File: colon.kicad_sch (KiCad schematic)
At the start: 10 parts, among them U42 SN74LVC244A

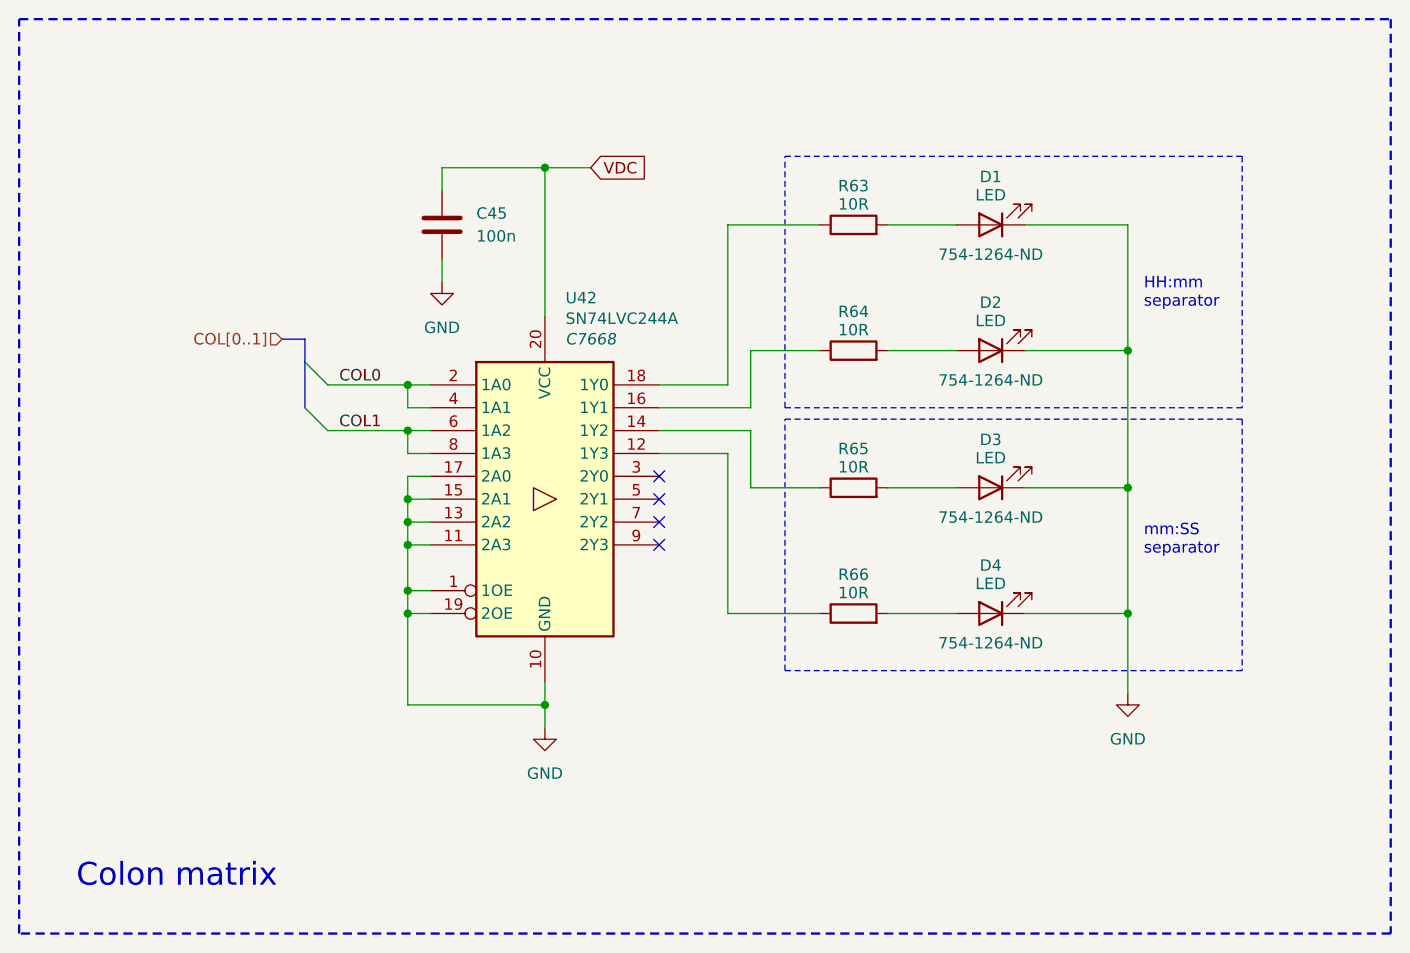
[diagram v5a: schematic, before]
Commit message: PCB routing
- JLCPCB constraints added
- removal of multiple test points
- change of footprints
- change of THT LEDs
- rough position of all the major components
- PCB routing started
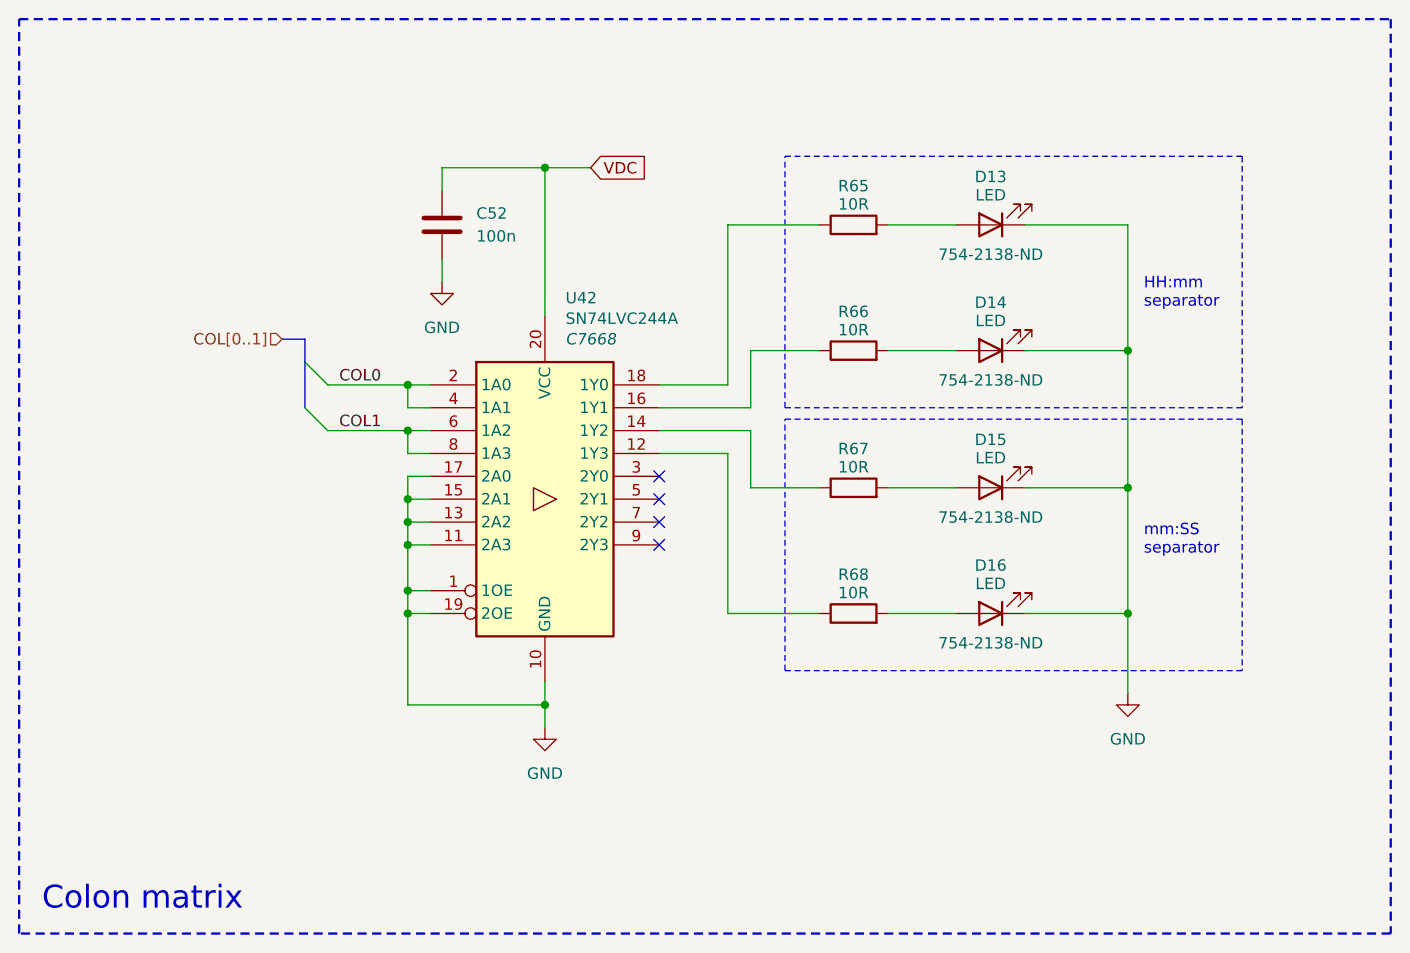
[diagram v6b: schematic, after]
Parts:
- removed D2, D3, D4: LED, LED_THT:LED_D5.0mm, symbol Device:LED
- added D14, D15, D16: LED, LED_THT:LED_D5.0mm, symbol Device:LED
- D13: renamed from D1; Digikey 754-1264-ND -> 754-2138-ND
- renumbered C45 to C52, R63 to R65, R64 to R66, R65 to R67, R66 to R68
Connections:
- net GND: now also D14.1 (K), D15.1 (K), D16.1 (K)
- net at R66.2: now also D14.2 (A)
- net at R67.2: now also D15.2 (A)
- net at R68.2: now also D16.2 (A)

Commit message: PCB routing
- addition of 3D models
- addition of docs
- reduction of the size of passives
- increase in size of traces
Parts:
- C52: footprint Capacitor_SMD:C_0603_1608Metric -> Capacitor_SMD:C_0402_1005Metric
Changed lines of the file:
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@@
 			)
 		)
-		(property "Footprint" "Capacitor_SMD:C_0603_1608Metric"
+		(property "Footprint" "Capacitor_SMD:C_0402_1005Metric"
 			(at 111.4552 77.47 0)
 			(effects

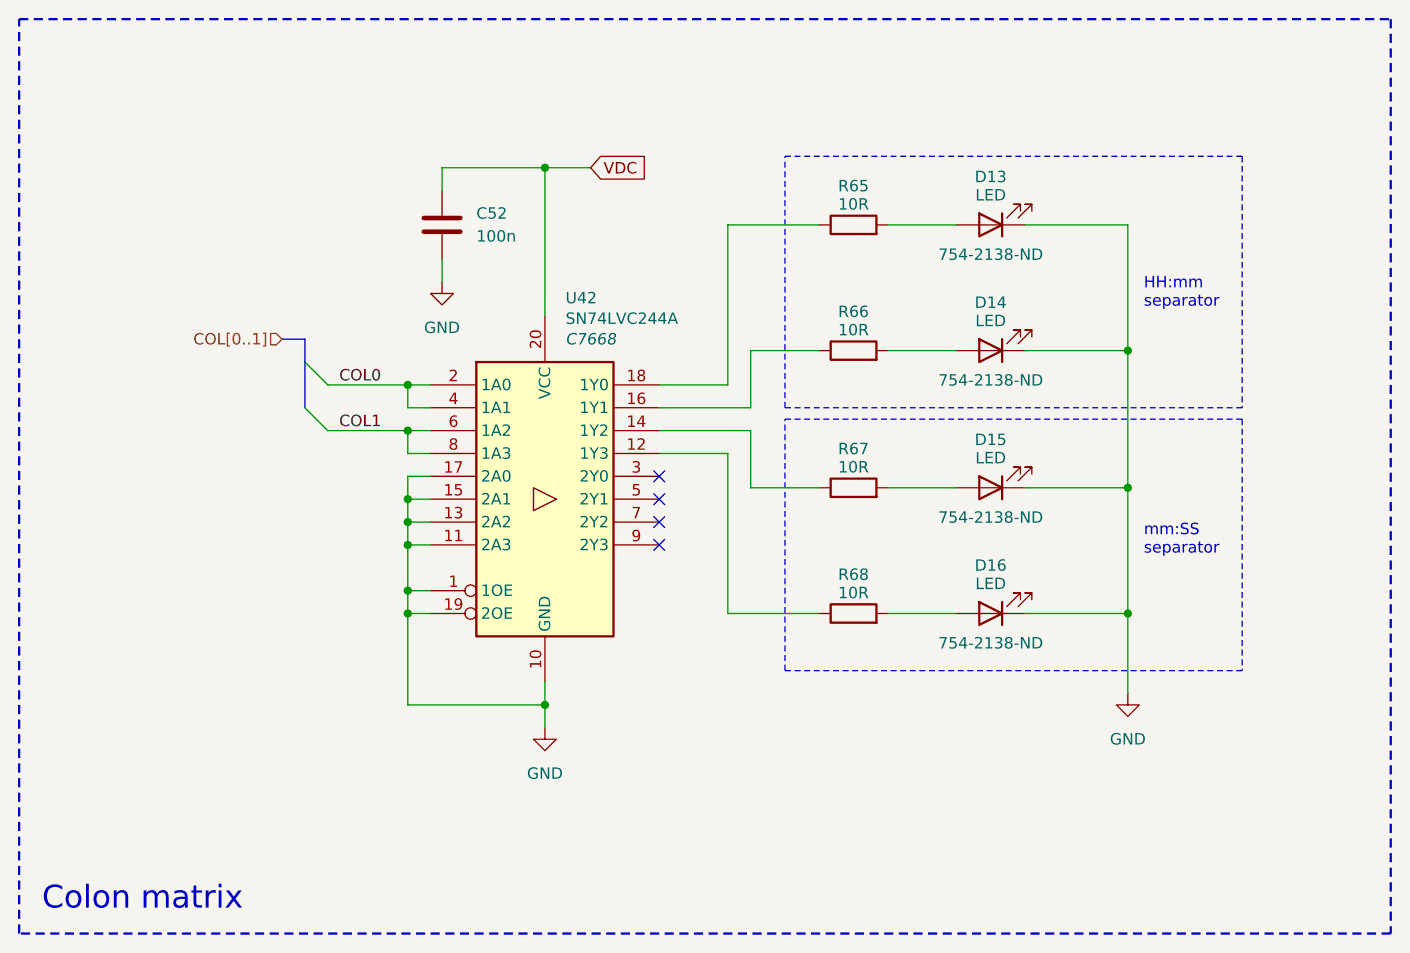
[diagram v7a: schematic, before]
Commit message: Primary MCU rerouting
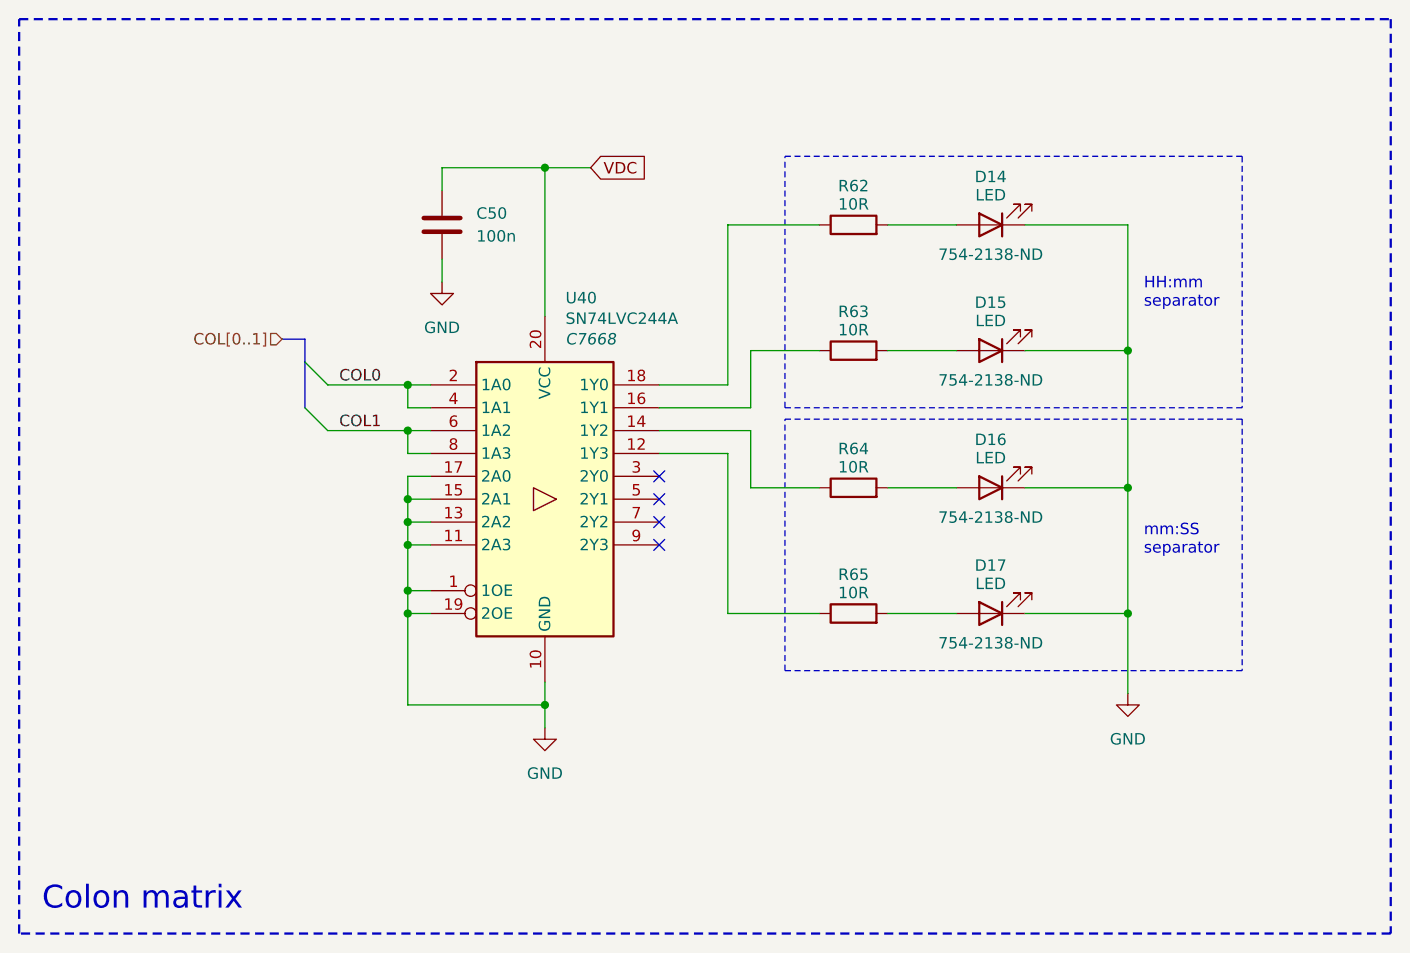
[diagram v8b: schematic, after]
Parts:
- renumbered C52 to C50, D13 to D14, D14 to D15, D15 to D16, D16 to D17, R65 to R62, R66 to R63, R67 to R64, R68 to R65, U42 to U40
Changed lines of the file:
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@@
 		(on_board yes)
 		(dnp no)
-		(property "Reference" "D16"
+		(property "Reference" "D17"
 			(at 171.45 111.506 0)
 			(effects
@@
 			(project "Precision Clock"
 				(path "/c9a8ff63-a0d1-4125-9dd1-40fb53daf536/9ee9cf55-854a-46a7-9bd0-7970985d5955"
-					(reference "D16")
+					(reference "D17")
 					(unit 1)
 				)
@@
 		(dnp no)
 		(fields_autoplaced yes)
-		(property "Reference" "#PWR0116"
+		(property "Reference" "#PWR0108"
 			(at 110.49 86.36 0)
 			(effects
@@
 			(project "Precision Clock"
 				(path "/c9a8ff63-a0d1-4125-9dd1-40fb53daf536/9ee9cf55-854a-46a7-9bd0-7970985d5955"
-					(reference "#PWR0116")
+					(reference "#PWR0108")
 					(unit 1)
 				)
@@
 		(on_board yes)
 		(dnp no)
-		(property "Reference" "D15"
+		(property "Reference" "D16"
 			(at 171.45 97.536 0)
 			(effects
@@
 			(project "Precision Clock"
 				(path "/c9a8ff63-a0d1-4125-9dd1-40fb53daf536/9ee9cf55-854a-46a7-9bd0-7970985d5955"
-					(reference "D15")
+					(reference "D16")
 					(unit 1)
 				)
@@
 		(on_board yes)
 		(dnp no)
-		(property "Reference" "R66"
+		(property "Reference" "R63"
 			(at 156.21 83.312 90)
 			(effects
@@
 			(project "Precision Clock"
 				(path "/c9a8ff63-a0d1-4125-9dd1-40fb53daf536/9ee9cf55-854a-46a7-9bd0-7970985d5955"
-					(reference "R66")
+					(reference "R63")
 					(unit 1)
 				)
@@
 		(on_board yes)
 		(dnp no)
-		(property "Reference" "D13"
+		(property "Reference" "D14"
 			(at 171.45 68.326 0)
 			(effects
@@
 			(project "Precision Clock"
 				(path "/c9a8ff63-a0d1-4125-9dd1-40fb53daf536/9ee9cf55-854a-46a7-9bd0-7970985d5955"
-					(reference "D13")
+					(reference "D14")
 					(unit 1)
 				)
@@
 		(on_board yes)
 		(dnp no)
-		(property "Reference" "U42"
+		(property "Reference" "U40"
 			(at 124.206 81.788 0)
 			(effects
@@
 			(project "Precision Clock"
 				(path "/c9a8ff63-a0d1-4125-9dd1-40fb53daf536/9ee9cf55-854a-46a7-9bd0-7970985d5955"
-					(reference "U42")
+					(reference "U40")
 					(unit 1)
 				)
@@
 		(dnp no)
 		(fields_autoplaced yes)
-		(property "Reference" "C52"
+		(property "Reference" "C50"
 			(at 114.3 72.3899 0)
 			(effects
@@
 			(project "Precision Clock"
 				(path "/c9a8ff63-a0d1-4125-9dd1-40fb53daf536/9ee9cf55-854a-46a7-9bd0-7970985d5955"
-					(reference "C52")
+					(reference "C50")
 					(unit 1)
 				)
@@
 		(on_board yes)
 		(dnp no)
-		(property "Reference" "R68"
+		(property "Reference" "R65"
 			(at 156.21 112.522 90)
 			(effects
@@
 			(project "Precision Clock"
 				(path "/c9a8ff63-a0d1-4125-9dd1-40fb53daf536/9ee9cf55-854a-46a7-9bd0-7970985d5955"
-					(reference "R68")
+					(reference "R65")
 					(unit 1)
 				)
@@
 		(on_board yes)
 		(dnp no)
-		(property "Reference" "D14"
+		(property "Reference" "D15"
 			(at 171.45 82.296 0)
 			(effects
@@
 			(project "Precision Clock"
 				(path "/c9a8ff63-a0d1-4125-9dd1-40fb53daf536/9ee9cf55-854a-46a7-9bd0-7970985d5955"
-					(reference "D14")
+					(reference "D15")
 					(unit 1)
 				)
@@
 		(dnp no)
 		(fields_autoplaced yes)
-		(property "Reference" "#PWR0117"
+		(property "Reference" "#PWR0109"
 			(at 121.92 135.89 0)
 			(effects
@@
 			(project "Precision Clock"
 				(path "/c9a8ff63-a0d1-4125-9dd1-40fb53daf536/9ee9cf55-854a-46a7-9bd0-7970985d5955"
-					(reference "#PWR0117")
+					(reference "#PWR0109")
 					(unit 1)
 				)
@@
 		(on_board yes)
 		(dnp no)
-		(property "Reference" "R67"
+		(property "Reference" "R64"
 			(at 156.21 98.552 90)
 			(effects
@@
 			(project "Precision Clock"
 				(path "/c9a8ff63-a0d1-4125-9dd1-40fb53daf536/9ee9cf55-854a-46a7-9bd0-7970985d5955"
-					(reference "R67")
+					(reference "R64")
 					(unit 1)
 				)
@@
 		(on_board yes)
 		(dnp no)
-		(property "Reference" "R65"
+		(property "Reference" "R62"
 			(at 156.21 69.342 90)
 			(effects
@@
 			(project "Precision Clock"
 				(path "/c9a8ff63-a0d1-4125-9dd1-40fb53daf536/9ee9cf55-854a-46a7-9bd0-7970985d5955"
-					(reference "R65")
+					(reference "R62")
 					(unit 1)
 				)
@@
 		(dnp no)
 		(fields_autoplaced yes)
-		(property "Reference" "#PWR0118"
+		(property "Reference" "#PWR0110"
 			(at 186.69 132.08 0)
 			(effects
@@
 			(project "Precision Clock"
 				(path "/c9a8ff63-a0d1-4125-9dd1-40fb53daf536/9ee9cf55-854a-46a7-9bd0-7970985d5955"
-					(reference "#PWR0118")
-					(unit 1)
-				)
+					(reference "#PWR0110")
+					(unit 1)
+				)
